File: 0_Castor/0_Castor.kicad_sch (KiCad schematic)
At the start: 3 parts, among them U1 Nice_Nano_V2, U2 RT9701, U3 AP9101CK

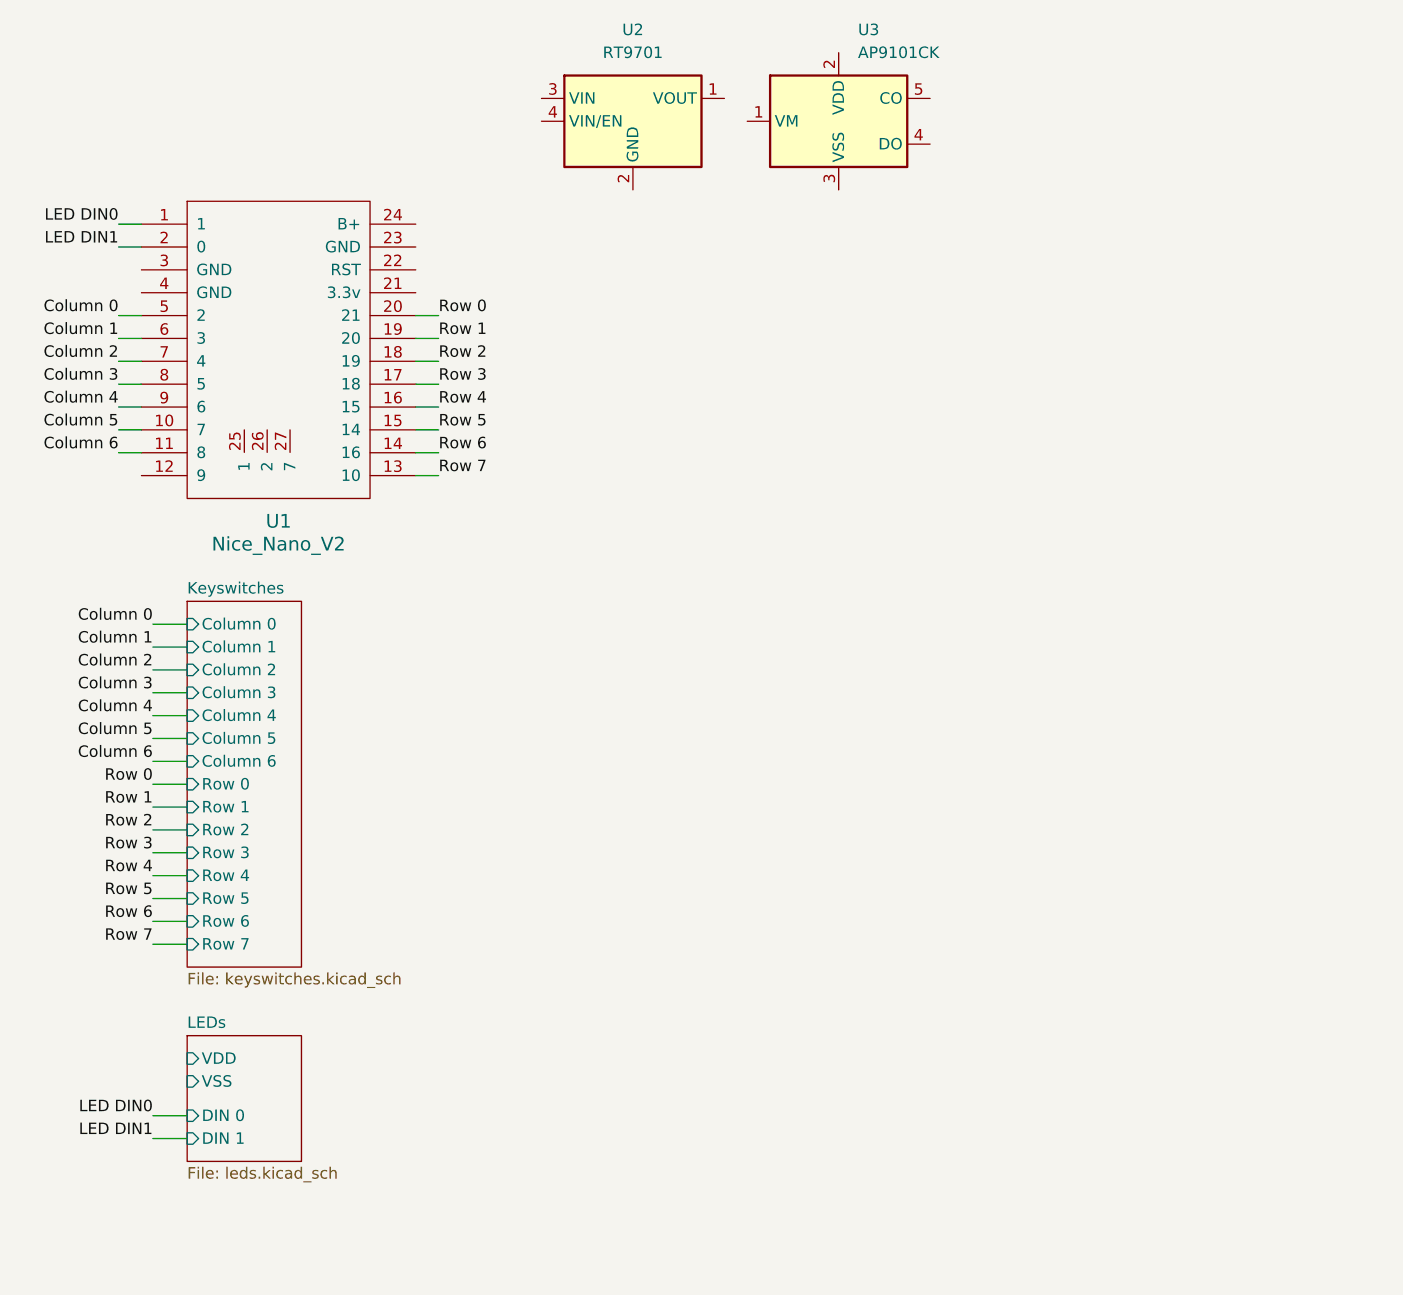
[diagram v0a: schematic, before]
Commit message: feat: add controller, battery jack, battery switch and reset switch placement
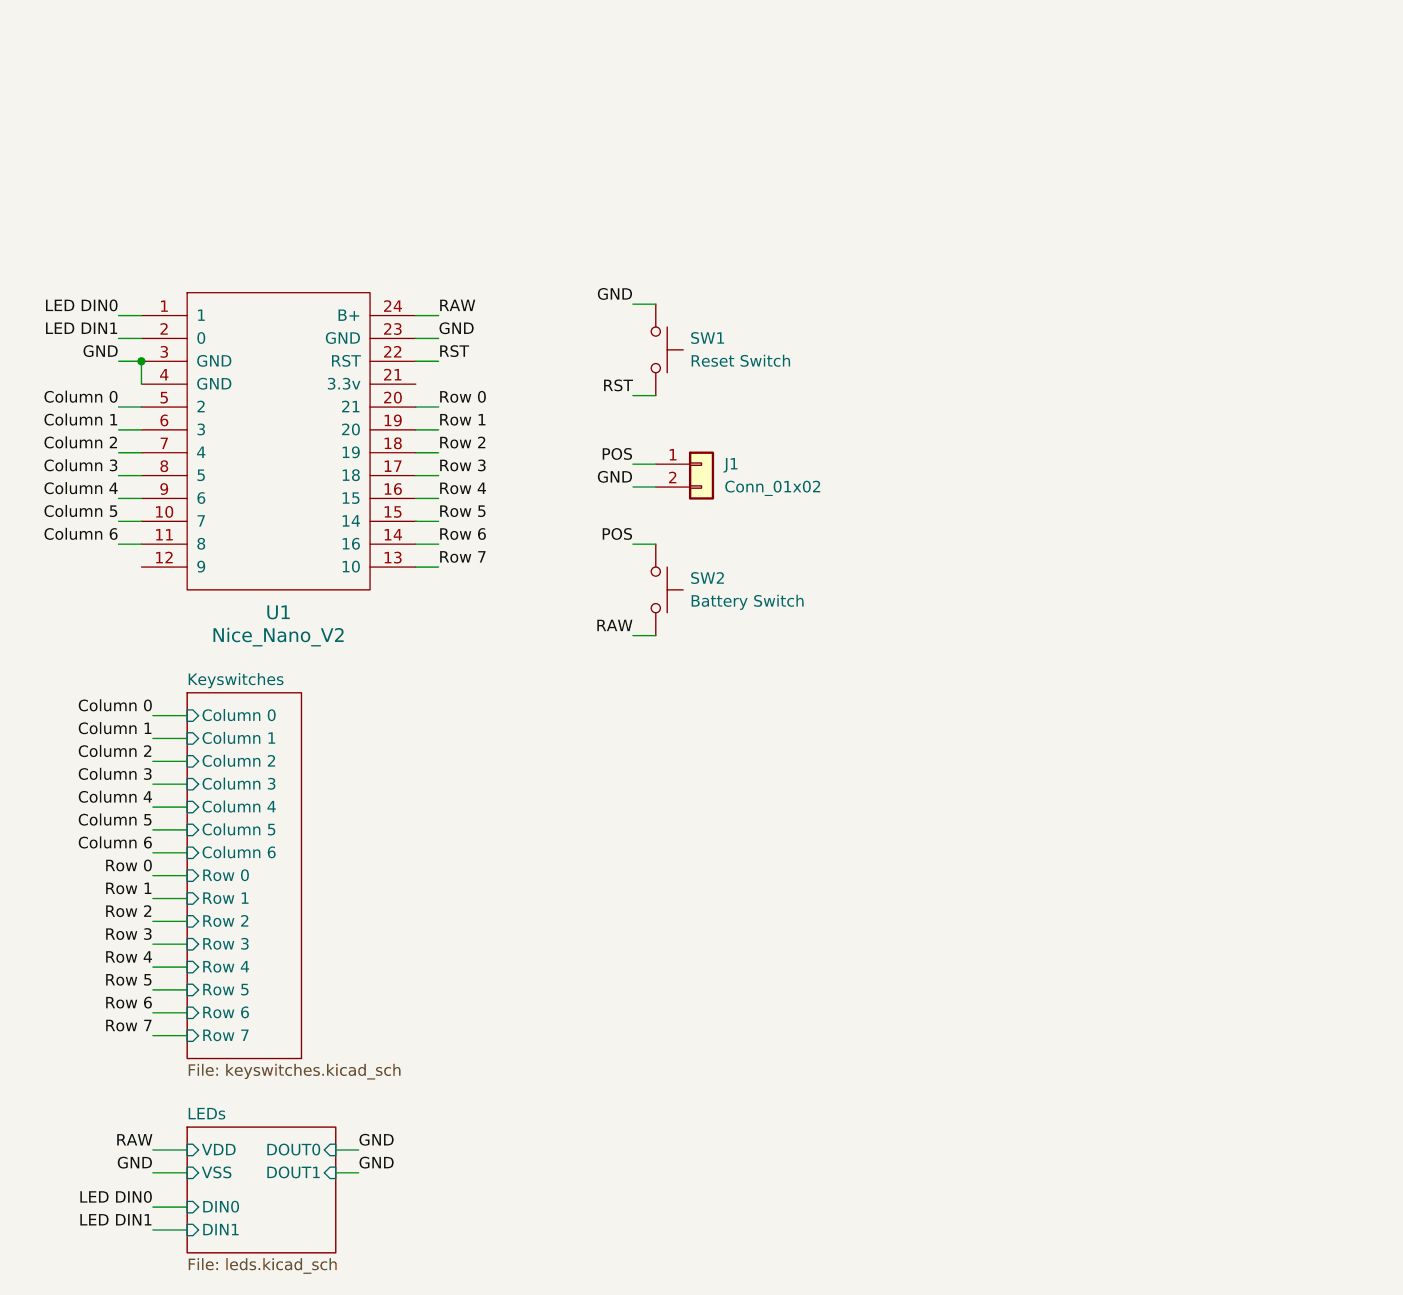
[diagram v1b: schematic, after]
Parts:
- removed U2: RT9701, Package_TO_SOT_SMD:TO-252-4, symbol Power_Management:RT9701
- removed U3: AP9101CK, Package_TO_SOT_SMD:SOT-23-5, symbol Battery_Management:AP9101CK
- added J1: Conn_01x02, Connector_JST:JST_PH_S2B-PH-K_1x02_P2.00mm_Horizontal, symbol Connector_Generic:Conn_01x02
- added SW1: Reset Switch, Button_Switch_SMD:Panasonic_EVQPUL_EVQPUC, symbol ScottoKeebs:Placeholder_Switch
- added SW2: Battery Switch, footprints:SPDT_C128955, symbol ScottoKeebs:Placeholder_Switch
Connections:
- net RST: now reaches U1.22 (RST)
- net RST: now also SW1.2
- net GND: now reaches U1.23 (GND)
- net GND: now also U1.3 (GND), U1.4 (GND), J1.2 (Pin_2), SW1.1
- net RAW: now reaches U1.24 (B+)
- net RAW: now also SW2.2
- new net POS: J1.1 (Pin_1), SW2.1
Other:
- sheet LEDs ports: added DIN0, DIN1, DOUT0, DOUT1; removed DIN 0, DIN 1

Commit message: feat: add LEDs, capacitors, resistors and rework schematic
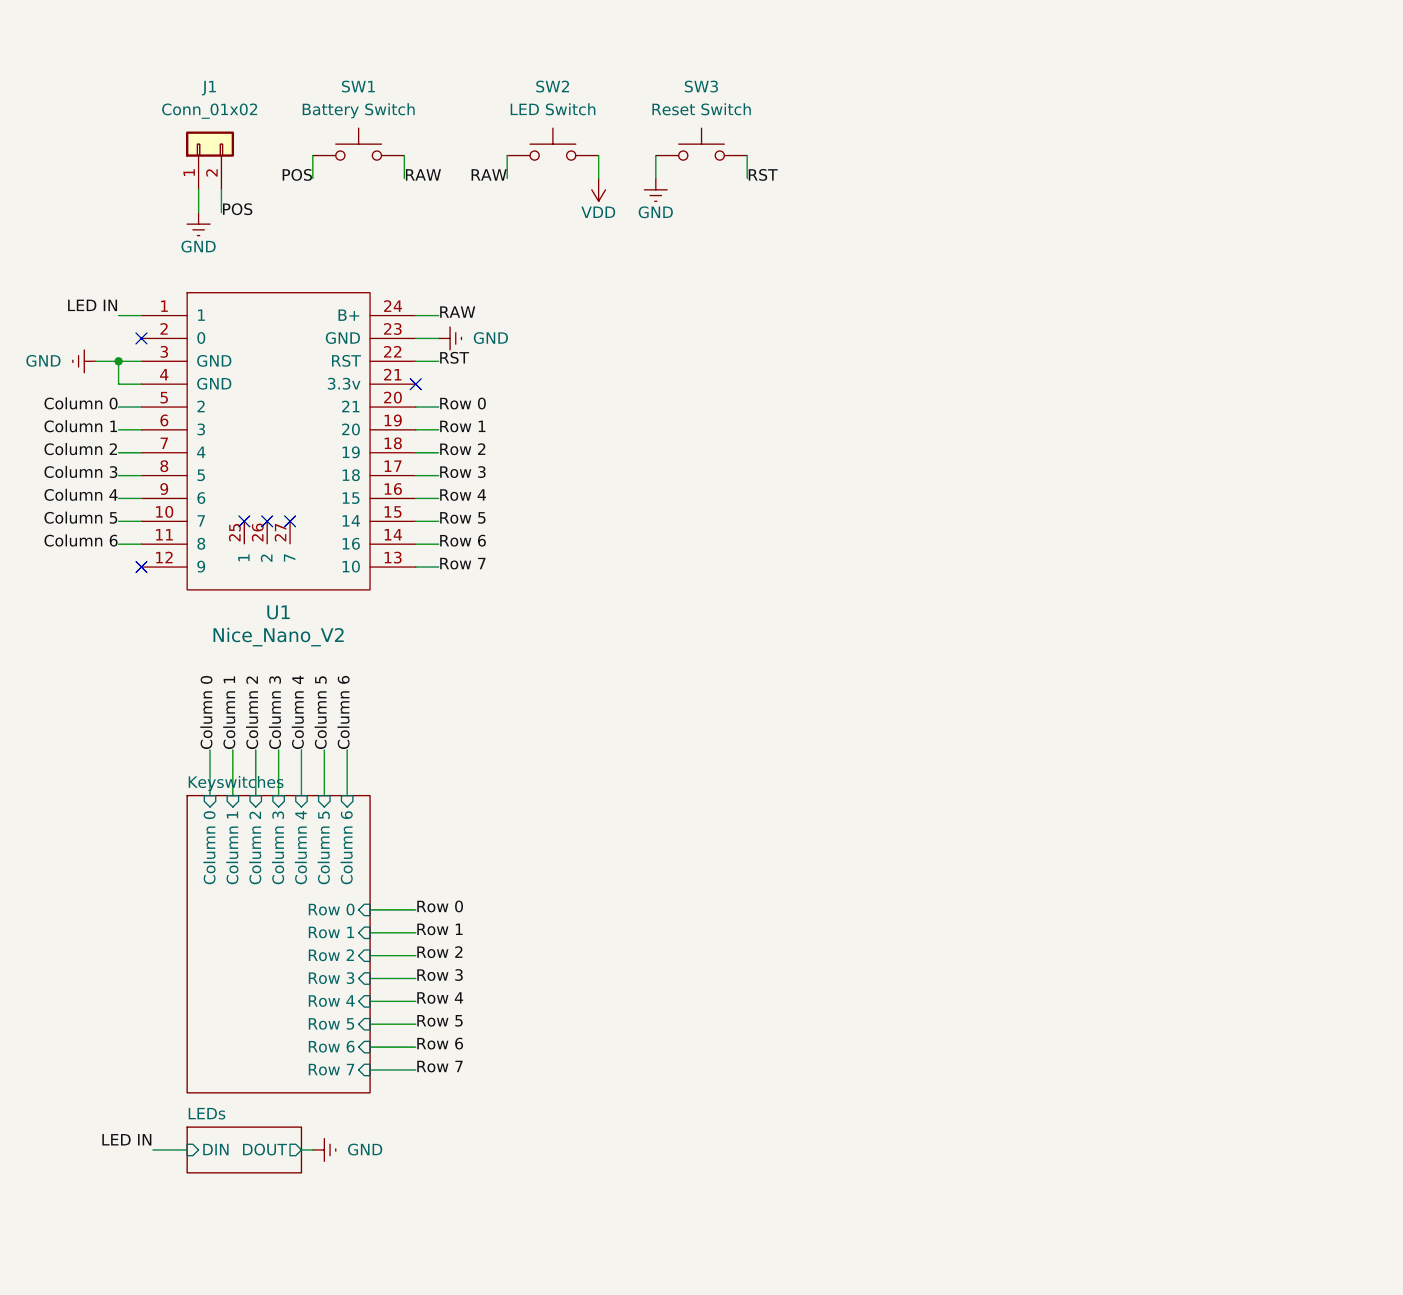
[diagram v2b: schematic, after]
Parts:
- added SW2: LED Switch, davidphilipbarr:SPDT_C128955, symbol ScottoKeebs:Placeholder_Switch
- SW1: renamed from SW2; footprint footprints:SPDT_C128955 -> davidphilipbarr:SPDT_C128955
- renumbered SW1 to SW3
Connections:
- net GND: now also J1.1 (Pin_1); no longer J1.2 (Pin_2)
- net POS: now also J1.2 (Pin_2); no longer J1.1 (Pin_1)
- net RAW: now also SW2.1
- net LED DIN0 renamed LED IN
- net LED DIN1: no longer names the net of U1.2 (0)
- new net VDD: SW2.2
- no-connect marks 0 -> 6
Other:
- sheet Keyswitches: file keyswitches.kicad_sch -> _keyswitches.kicad_sch
- sheet LEDs: file leds.kicad_sch -> _leds.kicad_sch
- sheet LEDs ports: added DIN, DOUT; removed DIN0, DIN1, DOUT0, DOUT1, VDD, VSS
- moved on the sheet: J1, SW1, SW3

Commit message: feat: convert 3.3V from nice!nano to 5V to LEDs
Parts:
- removed SW2: LED Switch, davidphilipbarr:SPDT_C128955, symbol ScottoKeebs:Placeholder_Switch
- renumbered SW3 to SW2
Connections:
- net +3.3V_{Nano}: now reaches U1.21 (3.3v)
- net LED IN renamed LED_{IN}
- net RAW renamed +3.7V
- no-connect marks 6 -> 2
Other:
- sheet LEDs ports: added D_{IN}, D_{OUT}; removed DIN, DOUT
- moved on the sheet: SW2

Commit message: feat: add voltage booster for LEDs power supply
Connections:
- net +3.7V renamed +3.7_{Battery}
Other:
- sheet LEDs ports: added LED_{IN}, LED_{OUT}; removed D_{IN}, D_{OUT}
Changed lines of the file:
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@@
 	(wire
 		(pts
-			(xy 165.1 44.45) (xy 166.37 44.45)
+			(xy 168.91 44.45) (xy 171.45 44.45)
 		)
 		(stroke
@@
 	(symbol
 		(lib_id "power:Earth")
-		(at 166.37 44.45 90)
+		(at 171.45 44.45 90)
 		(unit 1)
 		(body_style 1)
@@
 		(fields_autoplaced yes)
 		(property "Reference" "#PWR0102"
-			(at 172.72 44.45 0)
+			(at 177.8 44.45 0)
 			(hide yes)
 			(show_name no)
@@
 		)
 		(property "Value" "GND"
-			(at 170.18 44.4499 90)
+			(at 175.26 44.4499 90)
 			(show_name no)
 			(do_not_autoplace no)
@@
 		)
 		(property "Footprint" ""
-			(at 166.37 44.45 0)
+			(at 171.45 44.45 0)
 			(hide yes)
 			(show_name no)
@@
 		)
 		(property "Datasheet" ""
-			(at 166.37 44.45 0)
+			(at 171.45 44.45 0)
 			(hide yes)
 			(show_name no)
@@
 		)
 		(property "Description" "Power symbol creates a global label with name \"Earth\""
-			(at 166.37 44.45 0)
+			(at 171.45 44.45 0)
 			(hide yes)
 			(show_name no)
@@
 			)
 		)
-		(property "Value" "+3.7V"
+		(property "Value" "+3.7_{Battery}"
 			(at 77.47 44.4499 90)
 			(show_name no)
@@
 			)
 		)
-		(property "Value" "+3.7V"
+		(property "Value" "+3.7_{Battery}"
 			(at 71.12 34.29 0)
 			(show_name no)
@@
 	(sheet
 		(at 152.4 41.91)
-		(size 12.7 5.08)
+		(size 16.51 5.08)
 		(exclude_from_sim no)
 		(in_bom yes)
@@
 			)
 		)
-		(pin "D_{IN}" input
+		(pin "LED_{OUT}" output
+			(at 168.91 44.45 0)
+			(effects
+				(font
+					(size 1.27 1.27)
+				)
+				(justify right)
+			)
+		)
+		(pin "LED_{IN}" input
 			(at 152.4 44.45 180)
 			(effects
@@
 			)
 		)
-		(pin "D_{OUT}" output
-			(at 165.1 44.45 0)
-			(effects
-				(font
-					(size 1.27 1.27)
-				)
-				(justify right)
-			)
-		)

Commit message: feat: remove LED's and place components in PCB
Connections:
- net +3.3V_{Nano}: no longer names the net of U1.21 (3.3v)
- net LED_{IN}: no longer names the net of U1.1
- no-connect marks 2 -> 4
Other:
- removed sheet LEDs
